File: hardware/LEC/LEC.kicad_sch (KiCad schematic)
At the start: 37 parts, among them J1 54-00278, J10 Conn_01x02, J11 54-00278, J12 54-00278, J13 54-00278, J14 54-00278, J2 54-00278, J3 54-00278, J4 54-00278, J5 54-00278, J6 54-00278, J7 54-00278, J8 54-00278, J9 Conn_01x02, U1 Pico, U15 MCP3564RT-E/ST, U3 MC7809CTG, U4 W25Q128JVSIQ, U5 MAX31855KASA, U6 MAX31855KASA, U7 L7805

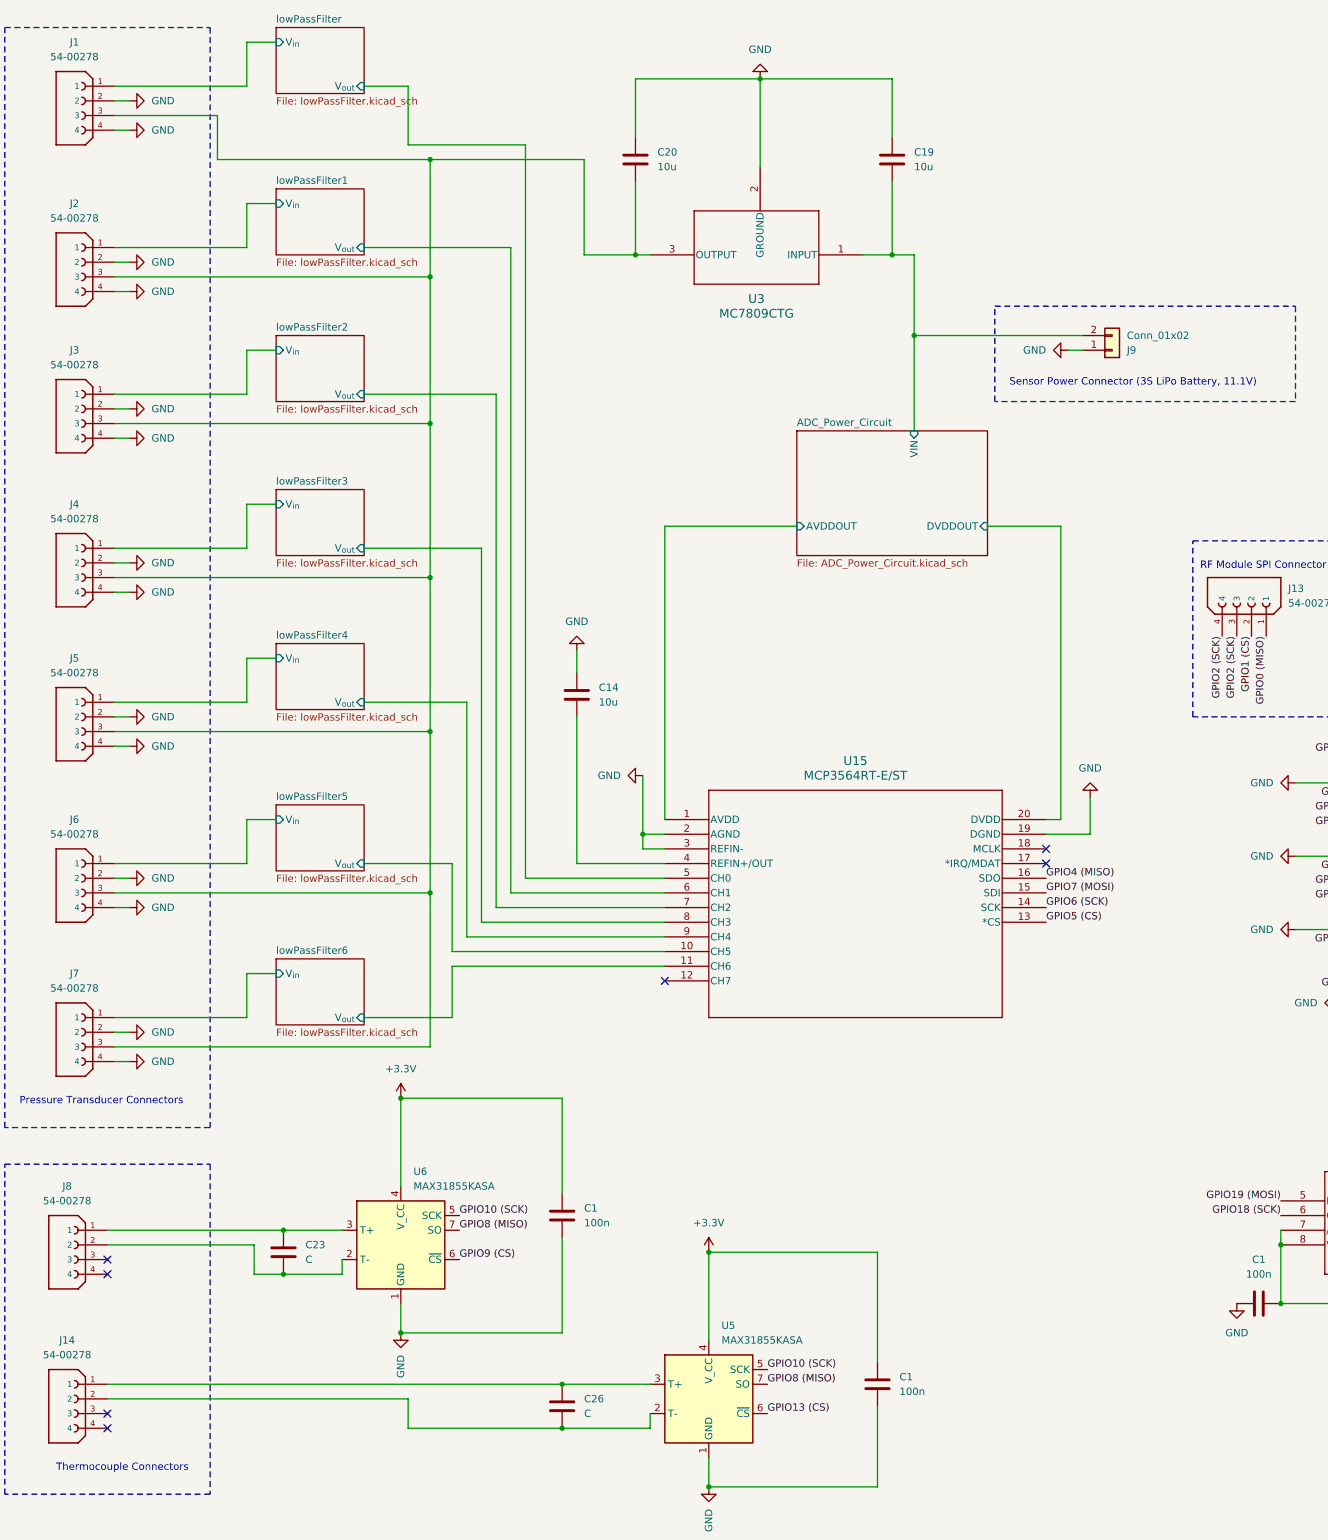
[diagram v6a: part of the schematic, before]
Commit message: Initial commit of PCB files, updated schematic syntax to smooth PCB design workflow. Need to fill ground planes and other necessary updates
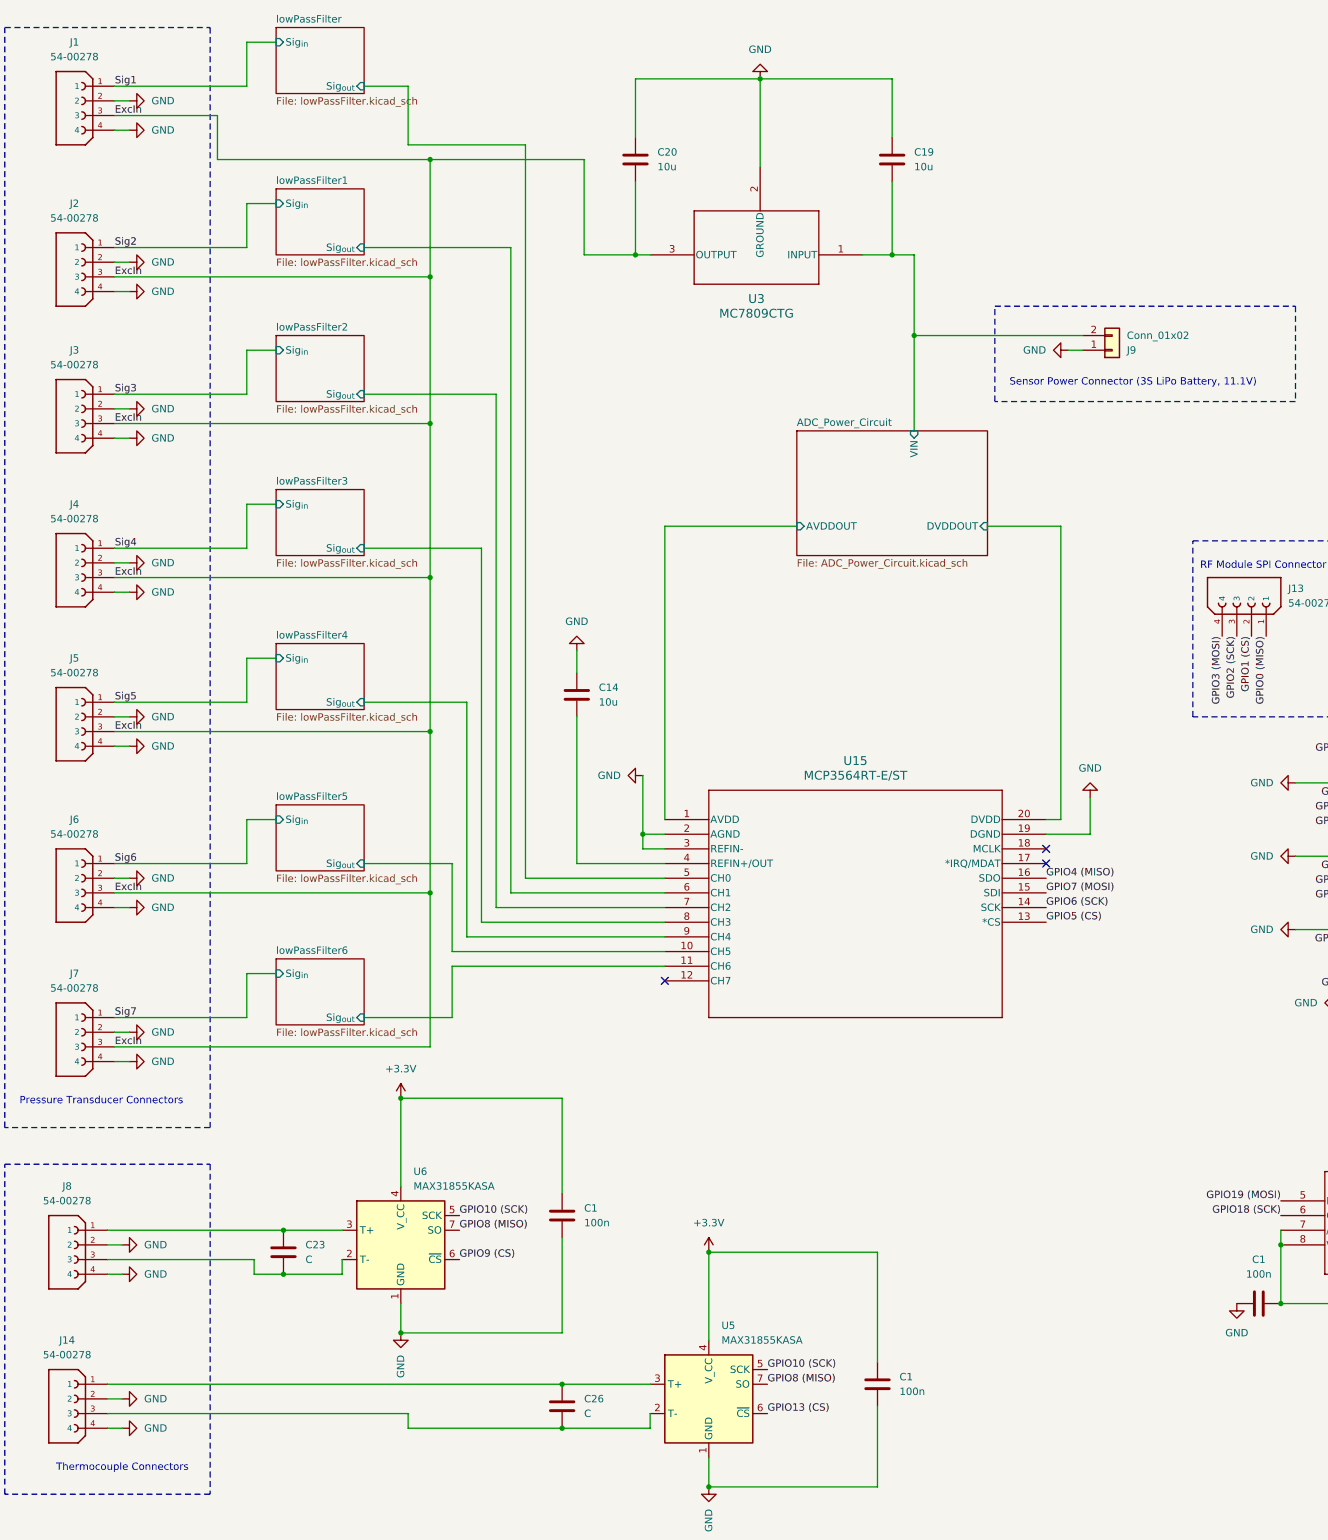
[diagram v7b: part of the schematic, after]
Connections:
- net GND: now also J14.2, J14.4, J8.2, J8.4
- net GPIO2 (SCK): no longer J13.4
- net GPIO3 (MOSI): now also J13.4
- net ExcIn: now reaches C20.2, J1.3, J2.3, J3.3, J4.3, J5.3, J6.3, J7.3, U3.3 (OUTPUT)
- net at C26.2, U5.2 (T-): now also J14.3; no longer J14.2
- net at C23.2, U6.2 (T-): now also J8.3; no longer J8.2
- net lowPassFilter/V_{in} renamed Sig1
- net lowPassFilter/V_{out} renamed lowPassFilter/Sig_{out}
- net lowPassFilter1/V_{in} renamed Sig2
- net lowPassFilter1/V_{out} renamed lowPassFilter1/Sig_{out}
- net lowPassFilter2/V_{in} renamed Sig3
- net lowPassFilter2/V_{out} renamed lowPassFilter2/Sig_{out}
- net lowPassFilter3/V_{in} renamed Sig4
- net lowPassFilter3/V_{out} renamed lowPassFilter3/Sig_{out}
- net lowPassFilter4/V_{in} renamed Sig5
- net lowPassFilter4/V_{out} renamed lowPassFilter4/Sig_{out}
- net lowPassFilter5/V_{in} renamed Sig6
- net lowPassFilter5/V_{out} renamed lowPassFilter5/Sig_{out}
- net lowPassFilter6/V_{in} renamed Sig7
- net lowPassFilter6/V_{out} renamed lowPassFilter6/Sig_{out}
- no-connect marks 23 -> 19
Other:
- sheet lowPassFilter ports: added Sig_{in}, Sig_{out}; removed V_{in}, V_{out}
- sheet lowPassFilter1 ports: added Sig_{in}, Sig_{out}; removed V_{in}, V_{out}
- sheet lowPassFilter2 ports: added Sig_{in}, Sig_{out}; removed V_{in}, V_{out}
- sheet lowPassFilter3 ports: added Sig_{in}, Sig_{out}; removed V_{in}, V_{out}
- sheet lowPassFilter4 ports: added Sig_{in}, Sig_{out}; removed V_{in}, V_{out}
- sheet lowPassFilter5 ports: added Sig_{in}, Sig_{out}; removed V_{in}, V_{out}
- sheet lowPassFilter6 ports: added Sig_{in}, Sig_{out}; removed V_{in}, V_{out}

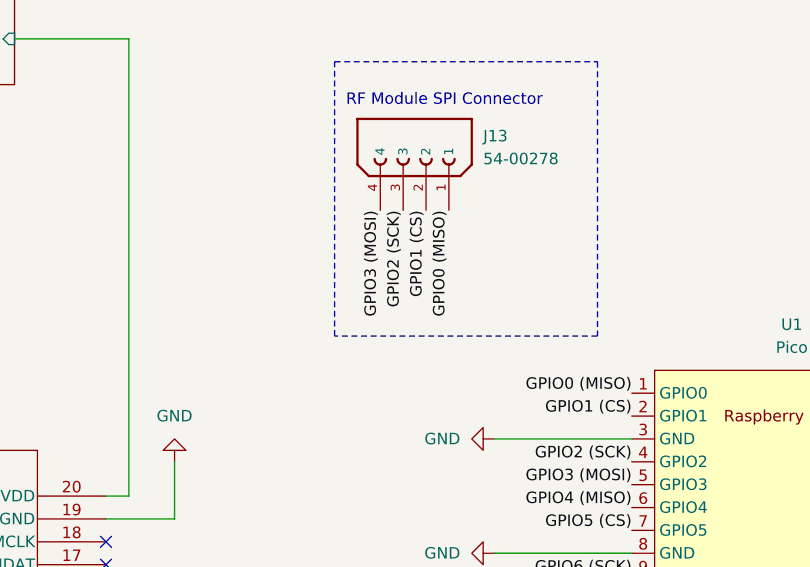
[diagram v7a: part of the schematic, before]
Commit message: Updated pin mapping of radio connector for cleaner routing
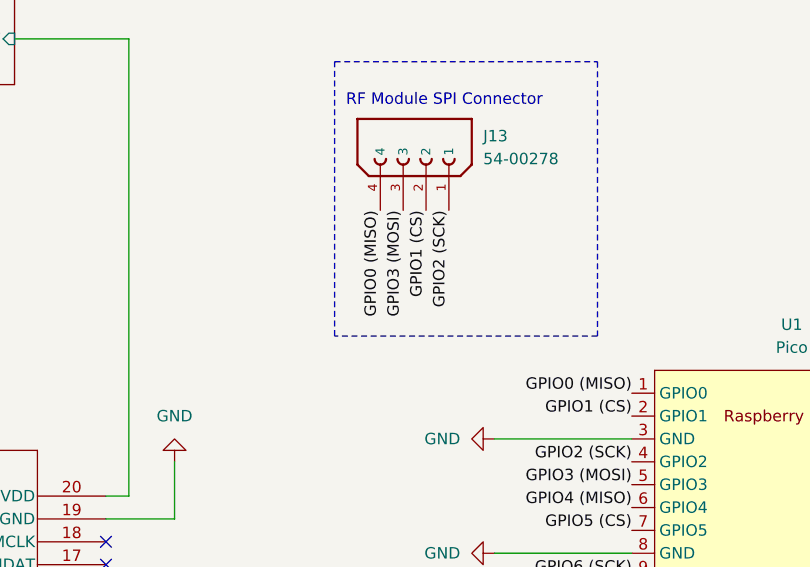
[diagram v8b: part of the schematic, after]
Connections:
- net GPIO0 (MISO): now also J13.4; no longer J13.1
- net GPIO2 (SCK): now also J13.1; no longer J13.3
- net GPIO3 (MOSI): now also J13.3; no longer J13.4
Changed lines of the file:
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@@
     (effects (font (size 1.27 1.27)) (justify left bottom))
+  )
+  (label "GPIO0 (MISO)" (at 241.3 124.46 270) (fields_autoplaced)
+    (effects (font (size 1.27 1.27)) (justify right bottom))
   )
   (label "GPIO8 (MISO)" (at 269.24 170.18 180) (fields_autoplaced)
@@
   (label "GPIO5 (CS)" (at 210.82 173.99 0) (fields_autoplaced)
     (effects (font (size 1.27 1.27)) (justify left bottom))
+  )
+  (label "GPIO1 (CS)" (at 246.38 124.46 270) (fields_autoplaced)
+    (effects (font (size 1.27 1.27)) (justify right bottom))
   )
   (label "GPIO18 (SCK)" (at 304.8 185.42 0) (fields_autoplaced)
@@
   )
   (label "GPIO6 (SCK)" (at 269.24 165.1 180) (fields_autoplaced)
-    (effects (font (size 1.27 1.27)) (justify right bottom))
-  )
-  (label "GPIO0 (MISO)" (at 248.92 124.46 270) (fields_autoplaced)
     (effects (font (size 1.27 1.27)) (justify right bottom))
   )
@@
   )
   (label "GPIO18 (SCK)" (at 251.46 224.79 180) (fields_autoplaced)
-    (effects (font (size 1.27 1.27)) (justify right bottom))
-  )
-  (label "GPIO2 (SCK)" (at 243.84 124.46 270) (fields_autoplaced)
     (effects (font (size 1.27 1.27)) (justify right bottom))
   )
@@
     (effects (font (size 1.27 1.27)) (justify right bottom))
   )
-  (label "GPIO3 (MOSI)" (at 241.3 124.46 270) (fields_autoplaced)
-    (effects (font (size 1.27 1.27)) (justify right bottom))
-  )
   (label "ExcIn" (at 49.53 168.91 0) (fields_autoplaced)
     (effects (font (size 1.27 1.27)) (justify left bottom))
-  )
-  (label "GPIO1 (CS)" (at 246.38 124.46 270) (fields_autoplaced)
-    (effects (font (size 1.27 1.27)) (justify right bottom))
   )
   (label "Sig1" (at 49.53 29.21 0) (fields_autoplaced)
@@
   (label "GPIO8 (MISO)" (at 109.22 227.33 0) (fields_autoplaced)
     (effects (font (size 1.27 1.27)) (justify left bottom))
+  )
+  (label "GPIO2 (SCK)" (at 248.92 124.46 270) (fields_autoplaced)
+    (effects (font (size 1.27 1.27)) (justify right bottom))
   )
   (label "Sig7" (at 49.53 190.5 0) (fields_autoplaced)
@@
     (effects (font (size 1.27 1.27)) (justify left bottom))
   )
+  (label "GPIO3 (MOSI)" (at 243.84 124.46 270) (fields_autoplaced)
+    (effects (font (size 1.27 1.27)) (justify right bottom))
+  )
   (label "GPIO10 (SCK)" (at 109.22 224.79 0) (fields_autoplaced)
